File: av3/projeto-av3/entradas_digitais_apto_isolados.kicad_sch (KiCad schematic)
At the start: 28 parts, among them J1 Screw_Terminal_01x02, J2 Screw_Terminal_01x02, J3 Screw_Terminal_01x02, J4 Screw_Terminal_01x02, U1 4N25, U2 4N25, U3 4N25, U4 4N25

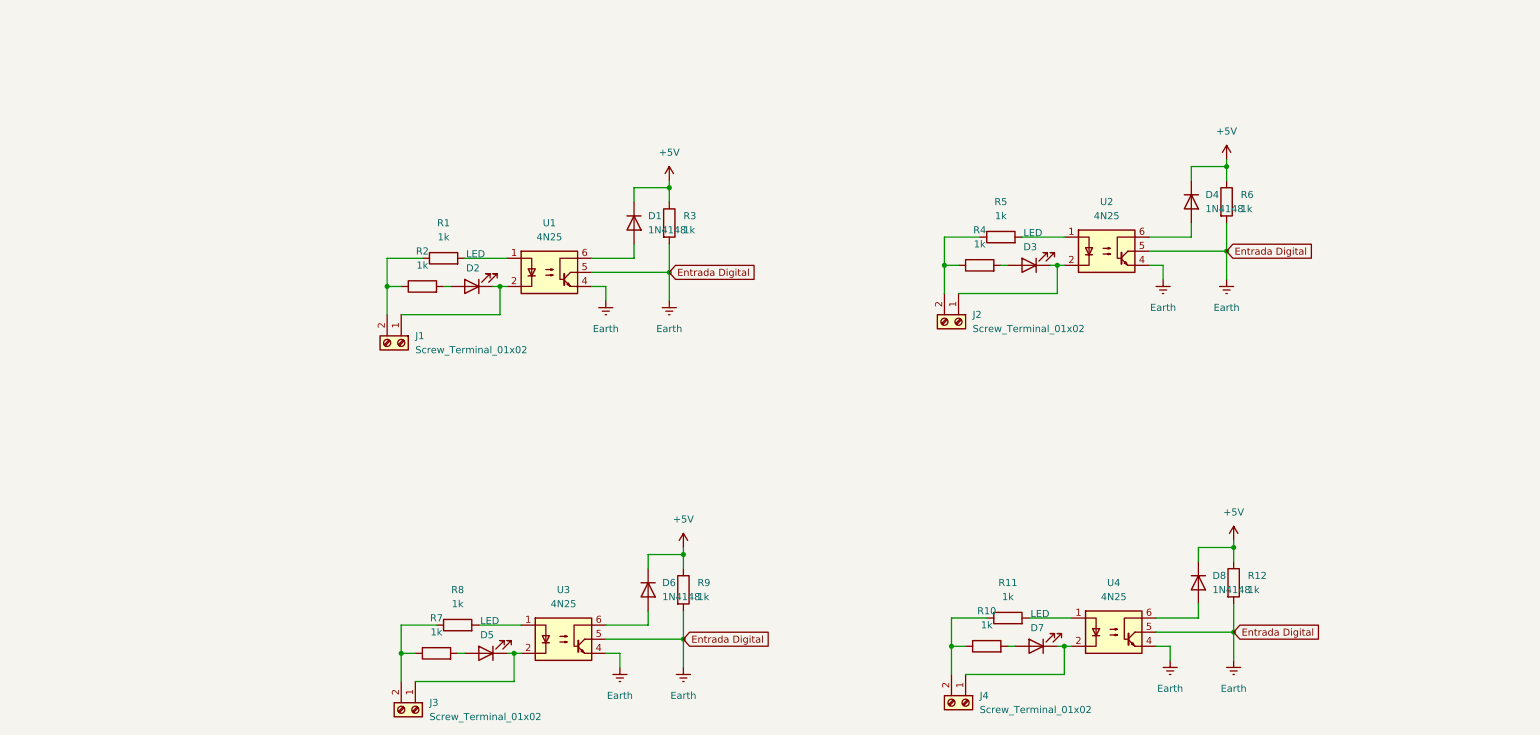
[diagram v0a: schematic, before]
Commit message: Maioria dos esquemáticos finalizados.
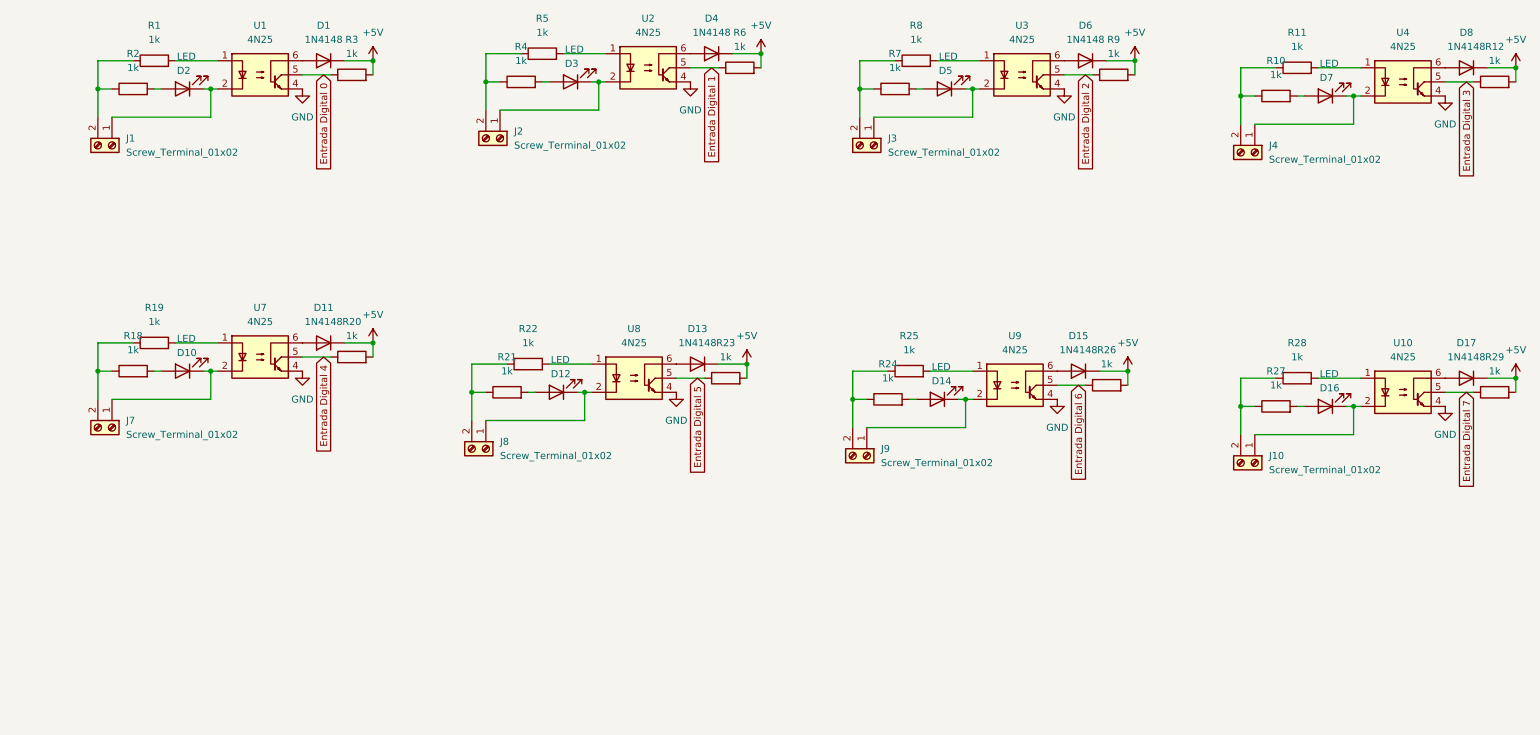
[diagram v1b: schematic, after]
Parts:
- added D10, D12, D14, D16: LED, symbol Device:LED
- added D11, D13, D15, D17: 1N4148, Diode_THT:D_DO-35_SOD27_P7.62mm_Horizontal, symbol Diode:1N4148
- added J10, J7, J8, J9: Screw_Terminal_01x02, symbol Connector:Screw_Terminal_01x02
- added R18, R19, R20, R21, R22, R23, R24, R25, R26, R27, R28, R29: 1k, symbol Device:R
- added U10, U7, U8, U9: 4N25, Package_DIP:DIP-6_W7.62mm, symbol Isolator:4N25
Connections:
- net +5V: now also R12.2, R3.2, R6.2, R9.2, D11.1 (K), D13.1 (K), D15.1 (K), D17.1 (K), R20.2, R23.2, R26.2, R29.2; no longer R12.1, R3.1, R6.1, R9.1
- removed net Earth: R12.2, R3.2, R6.2, R9.2, U1.4, U1.5, U2.4, U2.5, U3.4, U3.5, U4.4, U4.5
- new net: J10.2 (Pin_2), R27.1, R28.1
- new net: D16.2 (A), R27.2
- new net: D10.1 (K), J7.1 (Pin_1), U7.2
- new net: J7.2 (Pin_2), R18.1, R19.1
- new net: R19.2, U7.1
- new net: R25.2, U9.1
- new net: D14.1 (K), J9.1 (Pin_1), U9.2
- new net: D15.2 (A), U9.6
- new net: D12.1 (K), J8.1 (Pin_1), U8.2
- new net: J8.2 (Pin_2), R21.1, R22.1
- new net: D12.2 (A), R21.2
- new net: D11.2 (A), U7.6
- new net: D13.2 (A), U8.6
- new net: D17.2 (A), U10.6
- new net: J9.2 (Pin_2), R24.1, R25.1
- new net: D10.2 (A), R18.2
- new net: D14.2 (A), R24.2
- new net: D16.1 (K), J10.1 (Pin_1), U10.2
- new net: R22.2, U8.1
- new net: R28.2, U10.1
- new net Entrada Digital 0: R3.1, U1.5
- new net Entrada Digital 1: R6.1, U2.5
- new net Entrada Digital 2: R9.1, U3.5
- new net Entrada Digital 3: R12.1, U4.5
- new net Entrada Digital 4: R20.1, U7.5
- new net Entrada Digital 5: R23.1, U8.5
- new net Entrada Digital 6: R26.1, U9.5
- new net Entrada Digital 7: R29.1, U10.5
- new net GND: U1.4, U10.4, U2.4, U3.4, U4.4, U7.4, U8.4, U9.4
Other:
- moved on the sheet: D1, D2, J1, R1, R2, R3, U1

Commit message: Esquemático finalizado, faltando somente o PCB.
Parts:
- removed J1, J10, J2, J3, J4, J7, J8, J9: Screw_Terminal_01x02, symbol Connector:Screw_Terminal_01x02
- added J1, J19, J2, J3, J4, J7, J8, J9: Conn_01x02, TerminalBlock_Phoenix:TerminalBlock_Phoenix_MKDS-1,5-2_1x02_P5.00mm_Horizontal, symbol Connector_Generic:Conn_01x02
- D10, D12, D14, D16, D2, D3, D5, D7: footprint (none) -> LED_SMD:LED_1206_3216Metric
- R1, R11, R12, R19, R20, R22, R23, R25, R26, R28, R29, R3, R5, R6, R8, R9: value 1k -> 10k; footprint (none) -> Resistor_SMD:R_1206_3216Metric_Pad1.30x1.75mm_HandSolder
- R10, R18, R2, R21, R24, R27, R4, R7: footprint (none) -> Resistor_SMD:R_1206_3216Metric_Pad1.30x1.75mm_HandSolder
- U1, U10, U2, U3, U4, U7, U8, U9: footprint Package_DIP:DIP-6_W7.62mm -> Package_DIP:DIP-6_W7.62mm_SMDSocket_SmallPads
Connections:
- net at R27.1, R28.1: now also J9.1 (Pin_1)
- net at R7.1, R8.1: now also J4.1 (Pin_1)
- net at R10.1, R11.1: now also J8.1 (Pin_1)
- net at D10.1 (K), U7.2: now also J2.2 (Pin_2)
- net at R18.1, R19.1: now also J2.1 (Pin_1)
- net at D14.1 (K), U9.2: now also J7.2 (Pin_2)
- net at D12.1 (K), U8.2: now also J3.2 (Pin_2)
- net at R21.1, R22.1: now also J3.1 (Pin_1)
- net at R1.1, R2.1: now also J1.1 (Pin_1)
- net at D7.1 (K), U4.2: now also J8.2 (Pin_2)
- net at R4.1, R5.1: now also J19.1 (Pin_1)
- net at D3.1 (K), U2.2: now also J19.2 (Pin_2)
- net at D5.1 (K), U3.2: now also J4.2 (Pin_2)
- net at R24.1, R25.1: now also J7.1 (Pin_1)
- net at D16.1 (K), U10.2: now also J9.2 (Pin_2)
- net at D2.1 (K), U1.2: now also J1.2 (Pin_2)
- net Entrada Digital 0 renamed I.0
- net Entrada Digital 1 renamed I.1
- net Entrada Digital 2 renamed I.2
- net Entrada Digital 3 renamed I.3
- net Entrada Digital 4 renamed I.4
- net Entrada Digital 5 renamed I.5
- net Entrada Digital 6 renamed I.6
- net Entrada Digital 7 renamed I.7

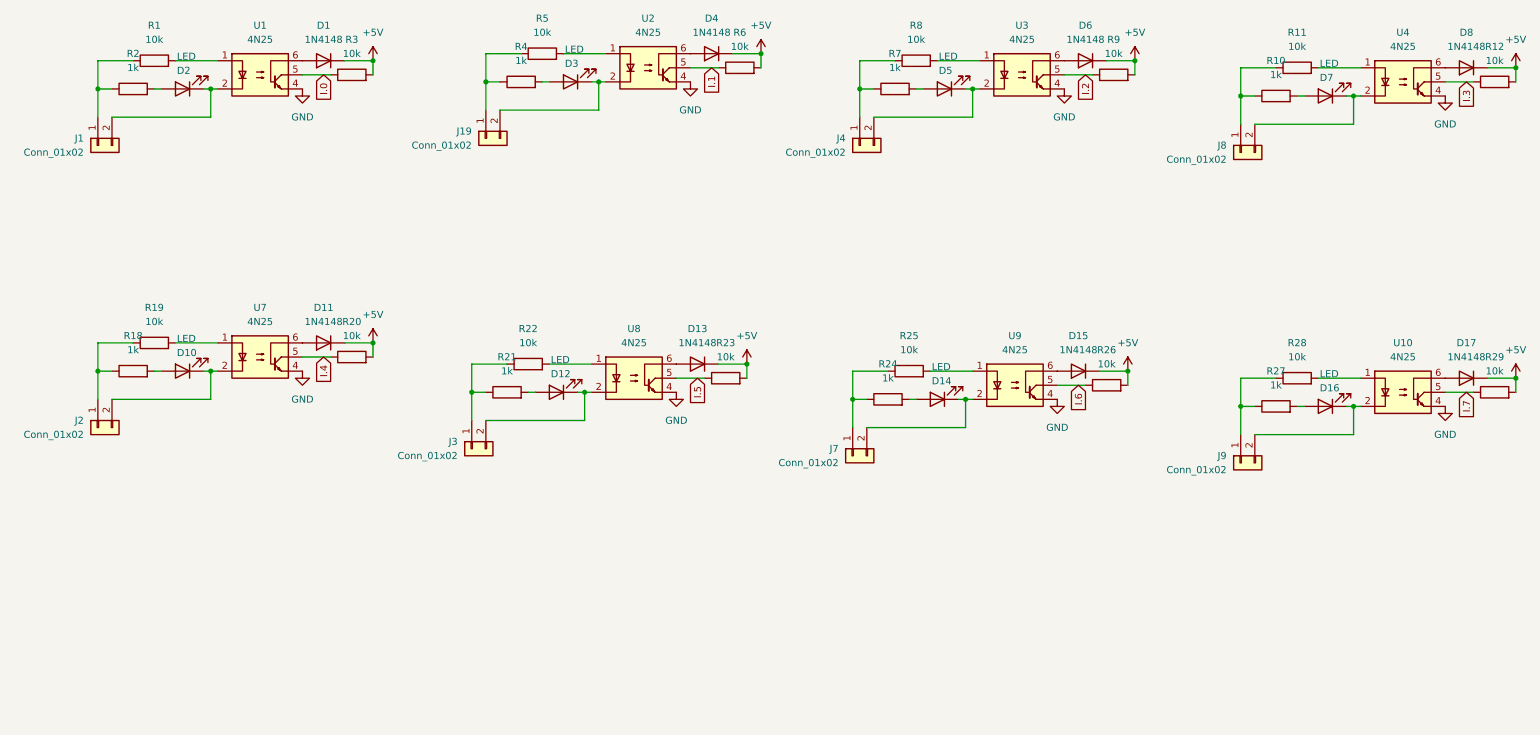
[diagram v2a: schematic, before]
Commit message: Referencias de componentes resetados; Progresso de 20% no PCB;
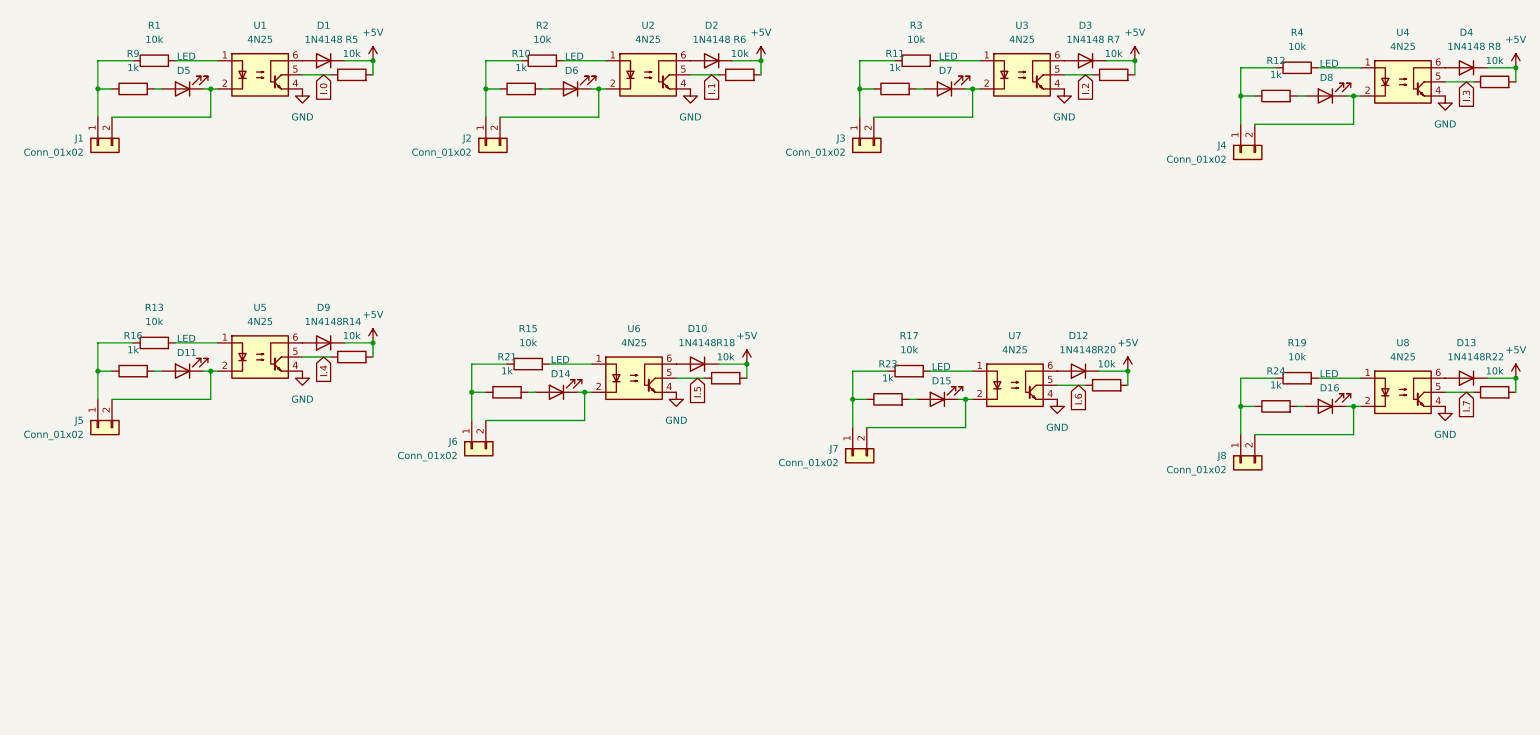
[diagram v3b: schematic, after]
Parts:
- renumbered D13 to D10, D10 to D11, D15 to D12, D17 to D13, D12 to D14, D14 to D15, D4 to D2, D6 to D3, D8 to D4, D2 to D5, D3 to D6, D5 to D7, D7 to D8, D11 to D9, J19 to J2, J4 to J3, J8 to J4, J2 to J5, J3 to J6, J9 to J8, R4 to R10, R7 to R11, R10 to R12, R19 to R13, R20 to R14, R22 to R15, R18 to R16, R25 to R17, R23 to R18, R28 to R19, R5 to R2, R26 to R20, R29 to R22, R24 to R23, R27 to R24, R8 to R3, R11 to R4, R3 to R5, R9 to R7, R12 to R8, R2 to R9, U7 to U5, U8 to U6, U9 to U7, U10 to U8
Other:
- moved on the sheet: D2, D6, J2, R10, R2, R6, U2
